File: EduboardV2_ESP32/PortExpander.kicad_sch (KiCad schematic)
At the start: 9 parts, among them U4 SX1509BIULTRT

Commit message: all parts placed. descision about usb-debug line to be made...
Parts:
- C2: footprint (none) -> Capacitor_SMD:C_0603_1608Metric
- JP5, JP6: footprint (none) -> Jumper:SolderJumper-2_P1.3mm_Open_RoundedPad1.0x1.5mm
- R17: footprint (none) -> Resistor_SMD:R_0603_1608Metric
- U4: footprint QFN-28_L4.0-W4.0-P0.40-BL-EP -> EduboardV2_kicadlib:QFN-28_L4.0-W4.0-P0.40-BL-EP; JLCPCB Part # (none) -> C128430
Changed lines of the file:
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@@
       (effects (font (size 1.27 1.27)))
     )
-    (property "Footprint" "" (at 154.432 46.355 90)
+    (property "Footprint" "Resistor_SMD:R_0603_1608Metric" (at 154.432 46.355 90)
       (effects (font (size 1.27 1.27)) hide)
     )
@@
       (effects (font (size 1.27 1.27)) (justify right) hide)
     )
-    (property "Footprint" "" (at 158.75 46.355 0)
+    (property "Footprint" "Jumper:SolderJumper-2_P1.3mm_Open_RoundedPad1.0x1.5mm" (at 158.75 46.355 0)
       (effects (font (size 1.27 1.27)) hide)
     )
@@
       (effects (font (size 1.27 1.27)) (justify left))
     )
-    (property "Footprint" "" (at 196.5198 78.74 0)
+    (property "Footprint" "Capacitor_SMD:C_0603_1608Metric" (at 196.5198 78.74 0)
       (effects (font (size 1.27 1.27)) hide)
     )
@@
       (effects (font (size 1.27 1.27)) (justify left))
     )
-    (property "Footprint" "QFN-28_L4.0-W4.0-P0.40-BL-EP" (at 158.75 125.73 0)
+    (property "Footprint" "EduboardV2_kicadlib:QFN-28_L4.0-W4.0-P0.40-BL-EP" (at 158.75 125.73 0)
       (effects (font (size 1.27 1.27)) hide)
     )
@@
     )
     (property "JLC Part" "Extended Part" (at 158.75 135.89 0)
+      (effects (font (size 1.27 1.27)) hide)
+    )
+    (property "JLCPCB Part #" "C128430" (at 158.75 95.25 0)
       (effects (font (size 1.27 1.27)) hide)
     )
@@
       (effects (font (size 1.27 1.27)) (justify right) hide)
     )
-    (property "Footprint" "" (at 158.75 139.7 0)
+    (property "Footprint" "Jumper:SolderJumper-2_P1.3mm_Open_RoundedPad1.0x1.5mm" (at 158.75 139.7 0)
       (effects (font (size 1.27 1.27)) hide)
     )
@@
       (effects (font (size 1.27 1.27)) (justify left))
     )
-    (property "Footprint" "" (at 165.4048 136.525 0)
+    (property "Footprint" "Capacitor_SMD:C_0603_1608Metric" (at 165.4048 136.525 0)
       (effects (font (size 1.27 1.27)) hide)
     )
@@
       (effects (font (size 1.27 1.27)) (justify left))
     )
-    (property "Footprint" "" (at 127.9398 78.74 0)
+    (property "Footprint" "Capacitor_SMD:C_0603_1608Metric" (at 127.9398 78.74 0)
       (effects (font (size 1.27 1.27)) hide)
     )
@@
       (effects (font (size 1.27 1.27)))
     )
-    (property "Footprint" "" (at 154.432 139.7 90)
+    (property "Footprint" "Resistor_SMD:R_0603_1608Metric" (at 154.432 139.7 90)
       (effects (font (size 1.27 1.27)) hide)
     )
@@
       (effects (font (size 1.27 1.27)) (justify left))
     )
-    (property "Footprint" "" (at 175.5648 136.525 0)
-      (effects (font (size 1.27 1.27)) hide)
-    )
+    (property "Footprint" "Capacitor_SMD:C_0603_1608Metric" (at 175.5648 136.525 0)
+      (effects (font (size 1.27 1.27)) hide)
+    )

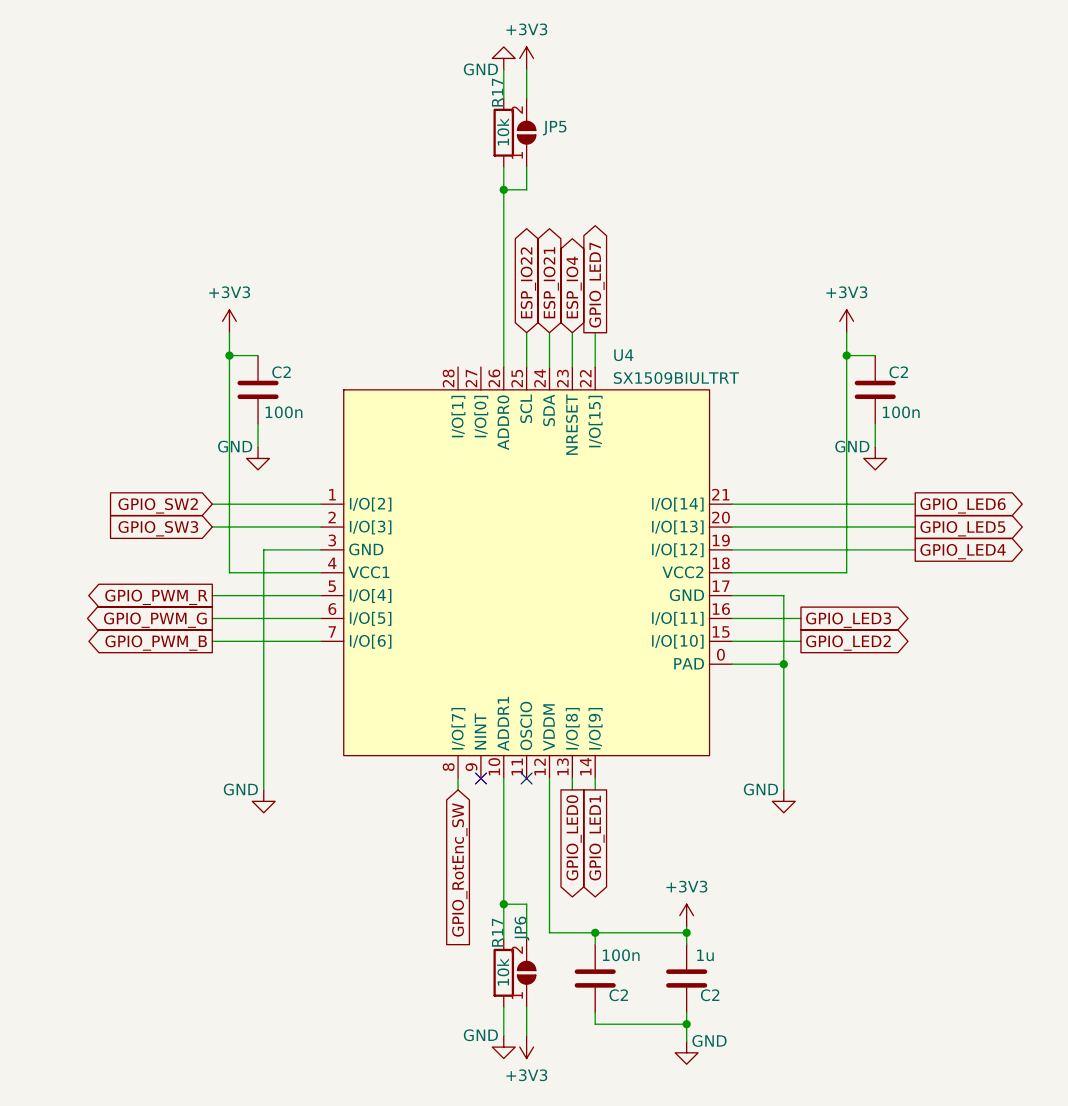
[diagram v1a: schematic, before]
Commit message: rework pin assignement with esp32 pin restrictions in mind. start layout
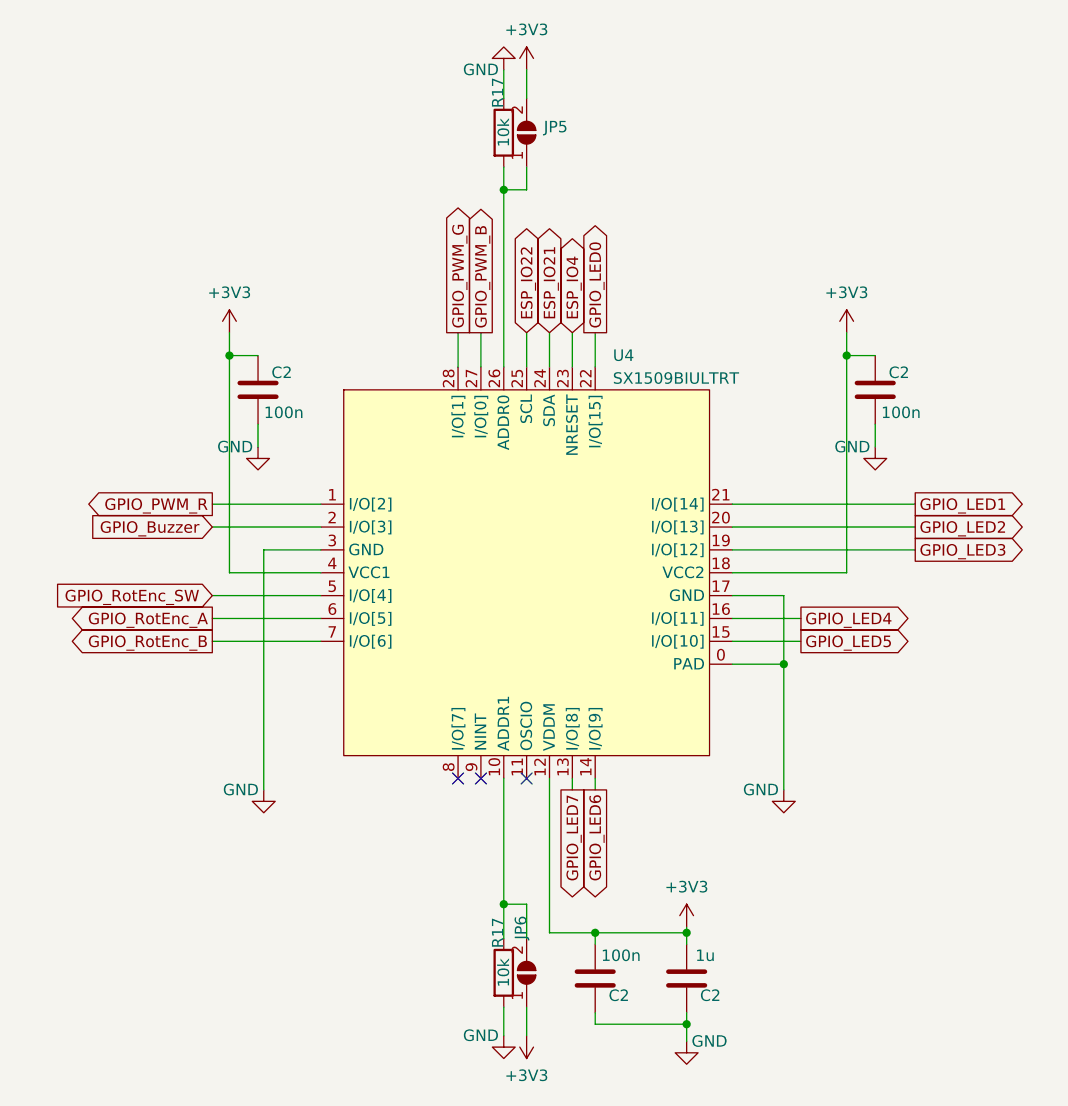
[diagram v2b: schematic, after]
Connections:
- net GPIO_SW2 is gone; now on net GPIO_PWM_R: U4.1 (I/O[2])
- net GPIO_LED0: now also U4.22 (I/O[15]); no longer U4.13 (I/O[8])
- net GPIO_LED1: now also U4.21 (I/O[14]); no longer U4.14 (I/O[9])
- net GPIO_LED2: now also U4.20 (I/O[13]); no longer U4.15 (I/O[10])
- net GPIO_LED3: now also U4.19 (I/O[12]); no longer U4.16 (I/O[11])
- net GPIO_LED4: now also U4.16 (I/O[11]); no longer U4.19 (I/O[12])
- net GPIO_LED5: now also U4.15 (I/O[10]); no longer U4.20 (I/O[13])
- net GPIO_LED6: now also U4.14 (I/O[9]); no longer U4.21 (I/O[14])
- net GPIO_LED7: now also U4.13 (I/O[8]); no longer U4.22 (I/O[15])
- net GPIO_PWM_B: now also U4.27 (I/O[0]); no longer U4.7 (I/O[6])
- net GPIO_PWM_G: now also U4.28 (I/O[1]); no longer U4.6 (I/O[5])
- net GPIO_PWM_R: no longer U4.5 (I/O[4])
- net GPIO_RotEnc_SW: now also U4.5 (I/O[4]); no longer U4.8 (I/O[7])
- net GPIO_SW3 renamed GPIO_Buzzer
- new net GPIO_RotEnc_A: U4.6 (I/O[5])
- new net GPIO_RotEnc_B: U4.7 (I/O[6])
- no-connect marks 2 -> 3
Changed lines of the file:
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@@
   (no_connect (at 158.75 118.11))
   (no_connect (at 153.67 118.11))
+  (no_connect (at 151.13 118.11))
   (wire (pts (xy 156.21 52.705) (xy 156.21 72.39))
     (stroke (width 0) (type default))
@@
     (stroke (width 0) (type default))
   )
+  (wire (pts (xy 151.13 68.58) (xy 151.13 72.39))
+    (stroke (width 0) (type default))
+  )
   (wire (pts (xy 156.21 50.165) (xy 156.21 52.705))
     (stroke (width 0) (type default))
@@
     (stroke (width 0) (type default))
   )
-  (wire (pts (xy 151.13 118.11) (xy 151.13 119.38))
-    (stroke (width 0) (type default))
-  )
   (wire (pts (xy 187.325 105.41) (xy 187.325 97.79))
     (stroke (width 0) (type default))
@@
     (stroke (width 0) (type default))
   )
+  (wire (pts (xy 153.67 68.58) (xy 153.67 72.39))
+    (stroke (width 0) (type default))
+  )
   (wire (pts (xy 158.75 132.08) (xy 158.75 135.89))
     (stroke (width 0) (type default))
@@
     )
   )
-  (global_label "GPIO_PWM_G" (shape output) (at 123.825 100.33 180) (fields_autoplaced)
-    (effects (font (size 1.27 1.27)) (justify right))
-    (property "Intersheetrefs" "${INTERSHEET_REFS}" (at 109.0659 100.33 0)
-      (effects (font (size 1.27 1.27)) (justify right) hide)
-    )
-  )
-  (global_label "GPIO_RotEnc_SW" (shape input) (at 151.13 119.38 270) (fields_autoplaced)
-    (effects (font (size 1.27 1.27)) (justify right))
-    (property "Intersheetrefs" "${INTERSHEET_REFS}" (at 151.13 137.8885 90)
-      (effects (font (size 1.27 1.27)) (justify right) hide)
-    )
-  )
-  (global_label "GPIO_PWM_R" (shape output) (at 123.825 97.79 180) (fields_autoplaced)
-    (effects (font (size 1.27 1.27)) (justify right))
-    (property "Intersheetrefs" "${INTERSHEET_REFS}" (at 109.0659 97.79 0)
-      (effects (font (size 1.27 1.27)) (justify right) hide)
-    )
-  )
-  (global_label "GPIO_PWM_B" (shape output) (at 123.825 102.87 180) (fields_autoplaced)
-    (effects (font (size 1.27 1.27)) (justify right))
-    (property "Intersheetrefs" "${INTERSHEET_REFS}" (at 109.0659 102.87 0)
-      (effects (font (size 1.27 1.27)) (justify right) hide)
-    )
-  )
-  (global_label "GPIO_LED7" (shape output) (at 166.37 68.58 90) (fields_autoplaced)
+  (global_label "GPIO_PWM_G" (shape output) (at 151.13 68.58 90) (fields_autoplaced)
+    (effects (font (size 1.27 1.27)) (justify left))
+    (property "Intersheetrefs" "${INTERSHEET_REFS}" (at 151.13 53.8209 90)
+      (effects (font (size 1.27 1.27)) (justify left) hide)
+    )
+  )
+  (global_label "GPIO_RotEnc_B" (shape output) (at 123.825 102.87 180) (fields_autoplaced)
+    (effects (font (size 1.27 1.27)) (justify right))
+    (property "Intersheetrefs" "${INTERSHEET_REFS}" (at 106.7074 102.87 0)
+      (effects (font (size 1.27 1.27)) (justify right) hide)
+    )
+  )
+  (global_label "GPIO_LED2" (shape output) (at 201.93 90.17 0) (fields_autoplaced)
+    (effects (font (size 1.27 1.27)) (justify left))
+    (property "Intersheetrefs" "${INTERSHEET_REFS}" (at 214.9353 90.17 0)
+      (effects (font (size 1.27 1.27)) (justify left) hide)
+    )
+  )
+  (global_label "GPIO_PWM_B" (shape output) (at 153.67 68.58 90) (fields_autoplaced)
+    (effects (font (size 1.27 1.27)) (justify left))
+    (property "Intersheetrefs" "${INTERSHEET_REFS}" (at 153.67 53.8209 90)
+      (effects (font (size 1.27 1.27)) (justify left) hide)
+    )
+  )
+  (global_label "GPIO_LED1" (shape output) (at 201.93 87.63 0) (fields_autoplaced)
+    (effects (font (size 1.27 1.27)) (justify left))
+    (property "Intersheetrefs" "${INTERSHEET_REFS}" (at 214.9353 87.63 0)
+      (effects (font (size 1.27 1.27)) (justify left) hide)
+    )
+  )
+  (global_label "GPIO_LED0" (shape output) (at 166.37 68.58 90) (fields_autoplaced)
     (effects (font (size 1.27 1.27)) (justify left))
     (property "Intersheetrefs" "${INTERSHEET_REFS}" (at 166.37 55.5747 90)
@@
     )
   )
-  (global_label "GPIO_LED0" (shape output) (at 163.83 119.38 270) (fields_autoplaced)
+  (global_label "GPIO_RotEnc_SW" (shape input) (at 123.825 97.79 180) (fields_autoplaced)
+    (effects (font (size 1.27 1.27)) (justify right))
+    (property "Intersheetrefs" "${INTERSHEET_REFS}" (at 105.3165 97.79 0)
+      (effects (font (size 1.27 1.27)) (justify right) hide)
+    )
+  )
+  (global_label "GPIO_LED5" (shape output) (at 189.23 102.87 0) (fields_autoplaced)
+    (effects (font (size 1.27 1.27)) (justify left))
+    (property "Intersheetrefs" "${INTERSHEET_REFS}" (at 202.2353 102.87 0)
+      (effects (font (size 1.27 1.27)) (justify left) hide)
+    )
+  )
+  (global_label "GPIO_LED4" (shape output) (at 189.23 100.33 0) (fields_autoplaced)
+    (effects (font (size 1.27 1.27)) (justify left))
+    (property "Intersheetrefs" "${INTERSHEET_REFS}" (at 202.2353 100.33 0)
+      (effects (font (size 1.27 1.27)) (justify left) hide)
+    )
+  )
+  (global_label "GPIO_Buzzer" (shape input) (at 123.825 90.17 180) (fields_autoplaced)
+    (effects (font (size 1.27 1.27)) (justify right))
+    (property "Intersheetrefs" "${INTERSHEET_REFS}" (at 109.1263 90.17 0)
+      (effects (font (size 1.27 1.27)) (justify right) hide)
+    )
+  )
+  (global_label "GPIO_LED3" (shape output) (at 201.93 92.71 0) (fields_autoplaced)
+    (effects (font (size 1.27 1.27)) (justify left))
+    (property "Intersheetrefs" "${INTERSHEET_REFS}" (at 214.9353 92.71 0)
+      (effects (font (size 1.27 1.27)) (justify left) hide)
+    )
+  )
+  (global_label "ESP_IO21" (shape bidirectional) (at 161.29 68.58 90) (fields_autoplaced)
+    (effects (font (size 1.27 1.27)) (justify left))
+    (property "Intersheetrefs" "${INTERSHEET_REFS}" (at 161.29 55.6125 90)
+      (effects (font (size 1.27 1.27)) (justify left) hide)
+    )
+  )
+  (global_label "ESP_IO4" (shape bidirectional) (at 163.83 68.58 90) (fields_autoplaced)
+    (effects (font (size 1.27 1.27)) (justify left))
+    (property "Intersheetrefs" "${INTERSHEET_REFS}" (at 163.83 56.822 90)
+      (effects (font (size 1.27 1.27)) (justify left) hide)
+    )
+  )
+  (global_label "GPIO_LED7" (shape output) (at 163.83 119.38 270) (fields_autoplaced)
     (effects (font (size 1.27 1.27)) (justify right))
     (property "Intersheetrefs" "${INTERSHEET_REFS}" (at 163.83 132.3853 90)
@@
     )
   )
-  (global_label "GPIO_LED6" (shape output) (at 201.93 87.63 0) (fields_autoplaced)
-    (effects (font (size 1.27 1.27)) (justify left))
-    (property "Intersheetrefs" "${INTERSHEET_REFS}" (at 214.9353 87.63 0)
-      (effects (font (size 1.27 1.27)) (justify left) hide)
-    )
-  )
-  (global_label "GPIO_SW2" (shape input) (at 123.825 87.63 180) (fields_autoplaced)
-    (effects (font (size 1.27 1.27)) (justify right))
-    (property "Intersheetrefs" "${INTERSHEET_REFS}" (at 111.6059 87.63 0)
-      (effects (font (size 1.27 1.27)) (justify right) hide)
-    )
-  )
-  (global_label "GPIO_LED2" (shape output) (at 189.23 102.87 0) (fields_autoplaced)
-    (effects (font (size 1.27 1.27)) (justify left))
-    (property "Intersheetrefs" "${INTERSHEET_REFS}" (at 202.2353 102.87 0)
-      (effects (font (size 1.27 1.27)) (justify left) hide)
-    )
-  )
-  (global_label "GPIO_SW3" (shape input) (at 123.825 90.17 180) (fields_autoplaced)
-    (effects (font (size 1.27 1.27)) (justify right))
-    (property "Intersheetrefs" "${INTERSHEET_REFS}" (at 111.6059 90.17 0)
-      (effects (font (size 1.27 1.27)) (justify right) hide)
-    )
-  )
-  (global_label "ESP_IO21" (shape bidirectional) (at 161.29 68.58 90) (fields_autoplaced)
-    (effects (font (size 1.27 1.27)) (justify left))
-    (property "Intersheetrefs" "${INTERSHEET_REFS}" (at 161.29 55.6125 90)
-      (effects (font (size 1.27 1.27)) (justify left) hide)
-    )
-  )
-  (global_label "ESP_IO4" (shape bidirectional) (at 163.83 68.58 90) (fields_autoplaced)
-    (effects (font (size 1.27 1.27)) (justify left))
-    (property "Intersheetrefs" "${INTERSHEET_REFS}" (at 163.83 56.822 90)
-      (effects (font (size 1.27 1.27)) (justify left) hide)
-    )
-  )
-  (global_label "GPIO_LED4" (shape output) (at 201.93 92.71 0) (fields_autoplaced)
-    (effects (font (size 1.27 1.27)) (justify left))
-    (property "Intersheetrefs" "${INTERSHEET_REFS}" (at 214.9353 92.71 0)
-      (effects (font (size 1.27 1.27)) (justify left) hide)
-    )
-  )
-  (global_label "GPIO_LED3" (shape output) (at 189.23 100.33 0) (fields_autoplaced)
-    (effects (font (size 1.27 1.27)) (justify left))
-    (property "Intersheetrefs" "${INTERSHEET_REFS}" (at 202.2353 100.33 0)
-      (effects (font (size 1.27 1.27)) (justify left) hide)
-    )
-  )
-  (global_label "GPIO_LED5" (shape output) (at 201.93 90.17 0) (fields_autoplaced)
-    (effects (font (size 1.27 1.27)) (justify left))
-    (property "Intersheetrefs" "${INTERSHEET_REFS}" (at 214.9353 90.17 0)
-      (effects (font (size 1.27 1.27)) (justify left) hide)
-    )
-  )
-  (global_label "GPIO_LED1" (shape output) (at 166.37 119.38 270) (fields_autoplaced)
+  (global_label "GPIO_RotEnc_A" (shape output) (at 123.825 100.33 180) (fields_autoplaced)
+    (effects (font (size 1.27 1.27)) (justify right))
+    (property "Intersheetrefs" "${INTERSHEET_REFS}" (at 106.8888 100.33 0)
+      (effects (font (size 1.27 1.27)) (justify right) hide)
+    )
+  )
+  (global_label "GPIO_PWM_R" (shape output) (at 123.825 87.63 180) (fields_autoplaced)
+    (effects (font (size 1.27 1.27)) (justify right))
+    (property "Intersheetrefs" "${INTERSHEET_REFS}" (at 109.0659 87.63 0)
+      (effects (font (size 1.27 1.27)) (justify right) hide)
+    )
+  )
+  (global_label "GPIO_LED6" (shape output) (at 166.37 119.38 270) (fields_autoplaced)
     (effects (font (size 1.27 1.27)) (justify right))
     (property "Intersheetrefs" "${INTERSHEET_REFS}" (at 166.37 132.3853 90)

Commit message: finalize Data. Add Logo and Text
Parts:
- C2: JLCPCB Part # (none) -> C105907; LCSC Part (none) -> C105907
- C2: JLCPCB Part # (none) -> C128624; LCSC Part (none) -> C128624
- R17: JLCPCB Part # (none) -> C116677; LCSC Part (none) -> C116677
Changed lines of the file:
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@@
+      (effects (font (size 1.27 1.27)) hide)
+    )
+    (property "JLCPCB Part #" "C116677" (at 156.21 46.355 0)
+      (effects (font (size 1.27 1.27)) hide)
+    )
+    (property "LCSC Part" "C116677" (at 156.21 46.355 0)
       (effects (font (size 1.27 1.27)) hide)
     )
@@
       (effects (font (size 1.27 1.27)) hide)
     )
-    (property "JLCPCB Part #" "" (at 197.485 74.93 0)
+    (property "JLCPCB Part #" "C105907" (at 197.485 74.93 0)
+      (effects (font (size 1.27 1.27)) hide)
+    )
+    (property "LCSC Part" "C105907" (at 197.485 74.93 0)
       (effects (font (size 1.27 1.27)) hide)
     )
@@
       (effects (font (size 1.27 1.27)) hide)
     )
-    (property "JLCPCB Part #" "" (at 166.37 140.335 0)
+    (property "JLCPCB Part #" "C105907" (at 166.37 140.335 0)
+      (effects (font (size 1.27 1.27)) hide)
+    )
+    (property "LCSC Part" "C105907" (at 166.37 140.335 0)
       (effects (font (size 1.27 1.27)) hide)
     )
@@
       (effects (font (size 1.27 1.27)) hide)
     )
-    (property "JLCPCB Part #" "" (at 128.905 74.93 0)
+    (property "JLCPCB Part #" "C105907" (at 128.905 74.93 0)
+      (effects (font (size 1.27 1.27)) hide)
+    )
+    (property "LCSC Part" "C105907" (at 128.905 74.93 0)
       (effects (font (size 1.27 1.27)) hide)
     )
@@
       (effects (font (size 1.27 1.27)) hide)
     )
+    (property "JLCPCB Part #" "C116677" (at 156.21 139.7 0)
+      (effects (font (size 1.27 1.27)) hide)
+    )
+    (property "LCSC Part" "C116677" (at 156.21 139.7 0)
+      (effects (font (size 1.27 1.27)) hide)
+    )
     (pin "1")
     (pin "2")
@@
       (effects (font (size 1.27 1.27)) hide)
     )
-    (property "JLCPCB Part #" "" (at 176.53 140.335 0)
-      (effects (font (size 1.27 1.27)) hide)
-    )
+    (property "JLCPCB Part #" "C128624" (at 176.53 140.335 0)
+      (effects (font (size 1.27 1.27)) hide)
+    )
+    (property "LCSC Part" "C128624" (at 176.53 140.335 0)
+      (effects (font (size 1.27 1.27)) hide)
+    )
